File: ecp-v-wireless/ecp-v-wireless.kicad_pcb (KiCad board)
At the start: 2 copper layers, 81.7 x 31.8 mm, 6 parts, among them U1 ESP32-S3-MINI-1, U2 LFE5U-85F-6BG381x

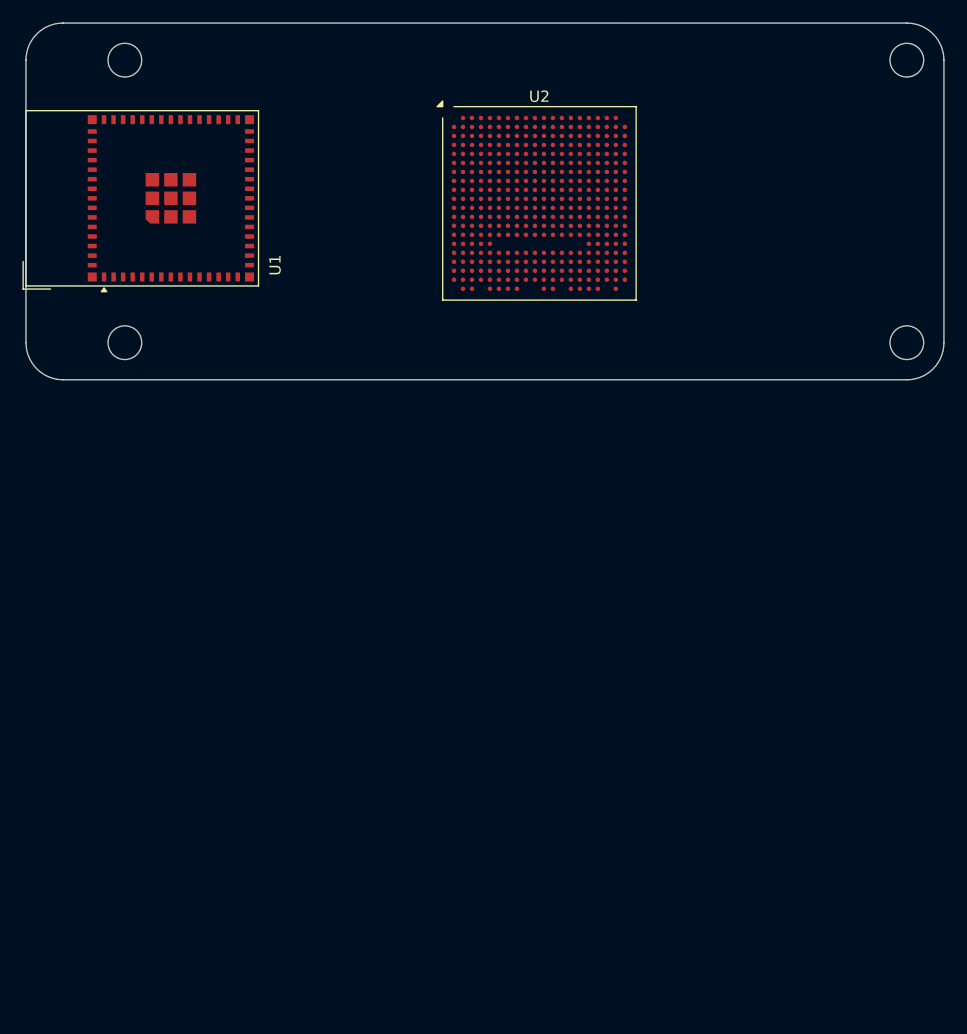
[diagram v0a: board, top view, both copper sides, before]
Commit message: Add block diagram, USB, LiPo MGMT, Regs, etc
Signed-off-by: Michael Welling <mwelling79@gmail.com>
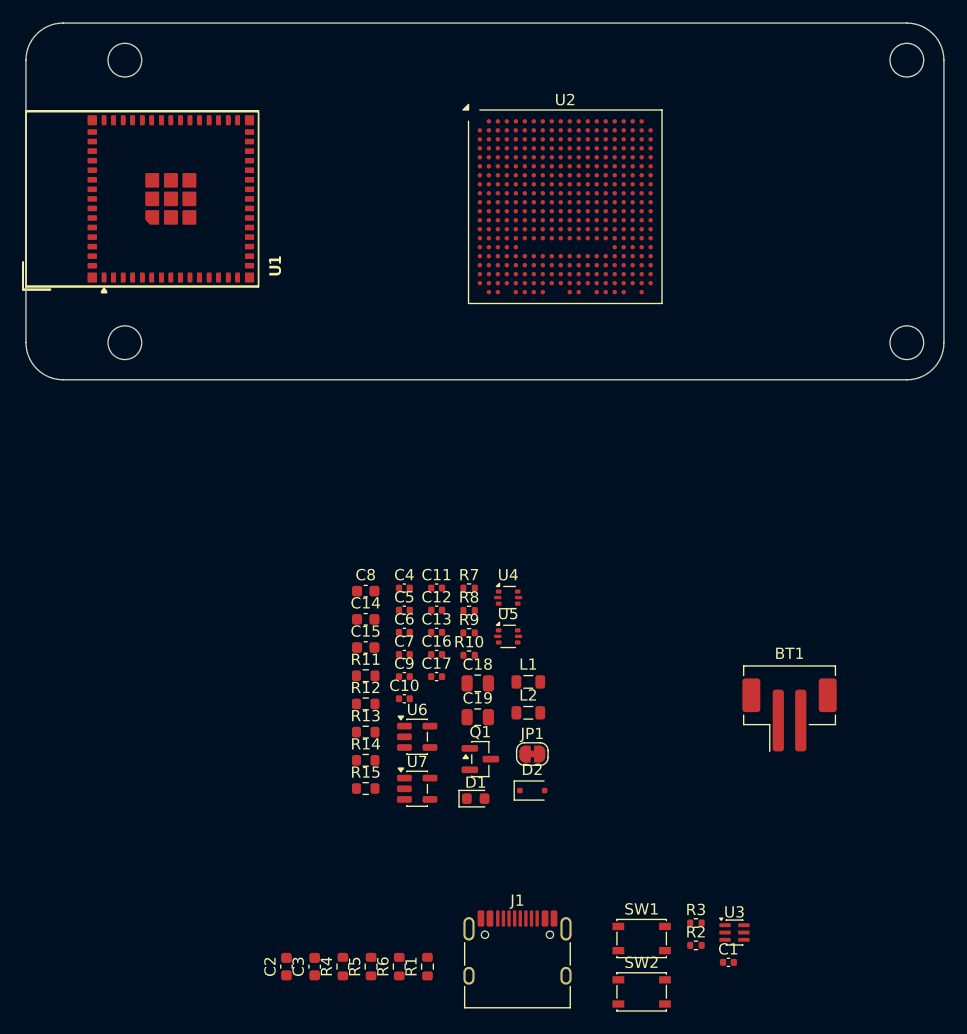
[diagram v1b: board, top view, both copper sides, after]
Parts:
- added BT1: Battery Connector, Connector_JST:JST_PH_B2B-PH-SM4-TB_1x02-1MP_P2.00mm_Vertical, F.Cu at (159.1, 142.1)
- added C1: 0.1uf, Capacitor_SMD:C_0402_1005Metric, F.Cu at (153.6, 164.2)
- added C10: 1uF, Capacitor_SMD:C_0402_1005Metric, F.Cu at (124.8, 140.7)
- added C11: 6.8pF, Capacitor_SMD:C_0402_1005Metric, F.Cu at (127.7, 130.8)
- added C12: 6.8pF, Capacitor_SMD:C_0402_1005Metric, F.Cu at (127.7, 132.8)
- added C13: 0.1uF, Capacitor_SMD:C_0402_1005Metric, F.Cu at (127.7, 134.8)
- added C14: 10uF, Capacitor_SMD:C_0603_1608Metric, F.Cu at (121.3, 133.6)
- added C15: 10uF, Capacitor_SMD:C_0603_1608Metric, F.Cu at (121.3, 136.1)
- added C16: 1uF, Capacitor_SMD:C_0402_1005Metric, F.Cu at (127.7, 136.8)
- added C17: 1uF, Capacitor_SMD:C_0402_1005Metric, F.Cu at (127.7, 138.7)
- added C18: 10uf, Capacitor_SMD:C_0805_2012Metric, F.Cu at (131.3, 139.3)
- added C19: 10uf, Capacitor_SMD:C_0805_2012Metric, F.Cu at (131.3, 142.3)
- added C2: 1uf, Capacitor_SMD:C_0603_1608Metric, F.Cu at (114.3, 164.5)
- added C3: 0.01uf, Capacitor_SMD:C_0603_1608Metric, F.Cu at (116.8, 164.5)
- added C4: 4.7uF, Capacitor_SMD:C_0402_1005Metric, F.Cu at (124.8, 130.8)
- added C5: 4.7uF, Capacitor_SMD:C_0402_1005Metric, F.Cu at (124.8, 132.8)
- added C6: 0.1uF, Capacitor_SMD:C_0402_1005Metric, F.Cu at (124.8, 134.8)
- added C7: 0.1uF, Capacitor_SMD:C_0402_1005Metric, F.Cu at (124.8, 136.8)
- added C8: 10uF, Capacitor_SMD:C_0603_1608Metric, F.Cu at (121.3, 131.1)
- added C9: 0.1uF, Capacitor_SMD:C_0402_1005Metric, F.Cu at (124.8, 138.7)
- added D1: LED Yellow, LED_SMD:LED_0603_1608Metric, F.Cu at (131.1, 149.6)
- added D2: PMEG3020EJ,115, Diode_SMD:D_SOD-323F, F.Cu at (136.2, 148.9)
- added J1: USB_C_Receptacle_USB2.0_16P, Connector_USB:USB_C_Receptacle_HRO_TYPE-C-31-M-12, F.Cu at (134.8, 164.3)
- added JP1: SolderJumper_2_Bridged, Jumper:SolderJumper-2_P1.3mm_Bridged_RoundedPad1.0x1.5mm, F.Cu at (136.2, 145.6)
- added L1: 2.2uH, Inductor_SMD:L_0805_2012Metric, F.Cu at (135.8, 139.2)
- added L2: 2.2uH, Inductor_SMD:L_0805_2012Metric, F.Cu at (135.8, 141.9)
- added Q1: DMP1045U-7, Package_TO_SOT_SMD:SOT-23, F.Cu at (131.5, 146.1)
- added R1: 10k, Resistor_SMD:R_0603_1608Metric, F.Cu at (126.8, 164.5)
- added R10: 100k, Resistor_SMD:R_0402_1005Metric, F.Cu at (130.5, 136.8)
- added R11: 10k, Resistor_SMD:R_0603_1608Metric, F.Cu at (121.3, 138.6)
- added R12: 10k, Resistor_SMD:R_0603_1608Metric, F.Cu at (121.3, 141.2)
- added R13: 1k, Resistor_SMD:R_0603_1608Metric, F.Cu at (121.3, 143.7)
- added R14: 100k, Resistor_SMD:R_0603_1608Metric, F.Cu at (121.3, 146.2)
- added R15: 100k, Resistor_SMD:R_0603_1608Metric, F.Cu at (121.3, 148.7)
- added R2: 27, Resistor_SMD:R_0402_1005Metric, F.Cu at (150.7, 162.6)
- added R3: 27, Resistor_SMD:R_0402_1005Metric, F.Cu at (150.7, 160.7)
- added R4: 5.1K, Resistor_SMD:R_0603_1608Metric, F.Cu at (119.3, 164.5)
- added R5: 5.1K, Resistor_SMD:R_0603_1608Metric, F.Cu at (121.8, 164.5)
- added R6: 1M, Resistor_SMD:R_0603_1608Metric, F.Cu at (124.3, 164.5)
- added R7: 210k, Resistor_SMD:R_0402_1005Metric, F.Cu at (130.5, 130.8)
- added R8: 47k, Resistor_SMD:R_0402_1005Metric, F.Cu at (130.5, 132.8)
- added R9: 84k5, Resistor_SMD:R_0402_1005Metric, F.Cu at (130.5, 134.8)
- added SW1: SW_Push, Button_Switch_SMD:SW_SPST_PTS810, F.Cu at (145.9, 162.0)
- added SW2: SW_Push, Button_Switch_SMD:SW_SPST_PTS810, F.Cu at (145.9, 166.8)
- added U1: ESP32-S3-MINI-1, RF_Module:ESP32-S2-MINI-1, F.Cu at (101.5, 96.2)
- added U3: DRTR5V0U4S, Package_TO_SOT_SMD:SOT-363_SC-70-6, F.Cu at (154.2, 161.5)
- added U4: TLV62569DRL, Package_TO_SOT_SMD:SOT-666, F.Cu at (134.0, 131.7)
- added U5: TLV62569DRL, Package_TO_SOT_SMD:SOT-666, F.Cu at (134.0, 135.1)
- added U6: TLV713285PDBV, Package_TO_SOT_SMD:SOT-23-5, F.Cu at (125.9, 144.1)
- added U7: MCP73831-2-OT, Package_TO_SOT_SMD:SOT-23-5, F.Cu at (125.9, 148.7)
- moved U2 2.32 mm to (139.1, 96.9)
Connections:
- net Net-(U2A-GND-PadB14) renamed GND
- net Net-(U2A-VCC-PadH10) renamed +1V1
- net Net-(U2A-VCCAUX-PadF15) renamed +2V5
